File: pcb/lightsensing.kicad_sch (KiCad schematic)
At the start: 5 parts, among them Q1 PNP

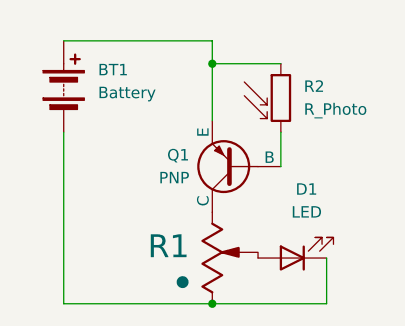
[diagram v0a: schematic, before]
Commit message: Added some silkscreen and weird looking design
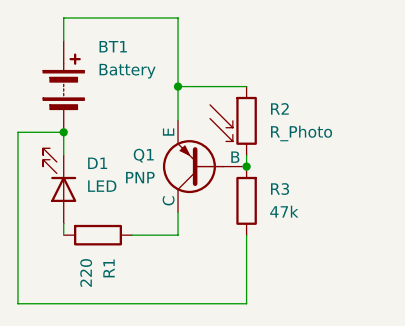
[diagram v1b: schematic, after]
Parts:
- removed R1: R-potentiometer,IEEE, pcb:TRIM_3362P-1-103, symbol PCM_Generic:R-potentiometer,IEEE
- added R1: 220, PCM_Resistor_THT_AKL:R_Axial_DIN0207_L6.3mm_D2.5mm_P2.54mm_Vertical, symbol Device:R
- added R3: 47k, PCM_Resistor_THT_AKL:R_Axial_DIN0207_L6.3mm_D2.5mm_P2.54mm_Vertical, symbol Device:R
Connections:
- net at BT1.2 (-), D1.1 (K): now also R3.1
- net at D1.2 (A): now also R1.2
- net at Q1.2 (B), R2.2: now also R3.2
- net at Q1.1 (C): now also R1.1
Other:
- moved on the sheet: D1, Q1, R2
